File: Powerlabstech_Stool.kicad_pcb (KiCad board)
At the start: 2 copper layers, 75 x 85 mm, 54 parts, among them J1 Screw_Terminal_01x02, J2 Conn_01x02_Pin, J3 Conn_01x02_Pin, J4 Conn_01x05_Socket, J5 Screw_Terminal_01x02, K1 SANYOU_SRD_Form_C, Q1 Q_NMOS_GSD, Q2 Q_NMOS_GSD, Q3 Q_NMOS_GSD, Q4 Q_NMOS_GSD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

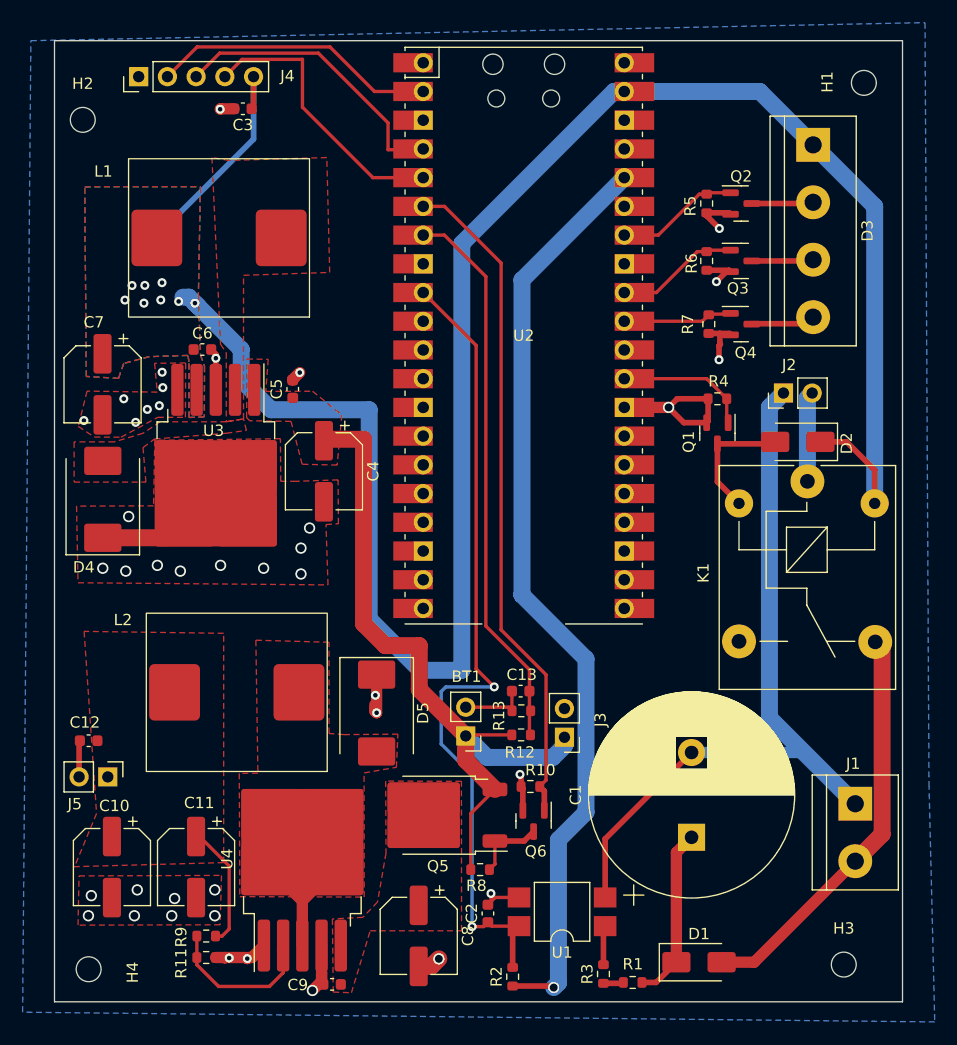
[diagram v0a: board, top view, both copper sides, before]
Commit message: Added the USB output and added the output files
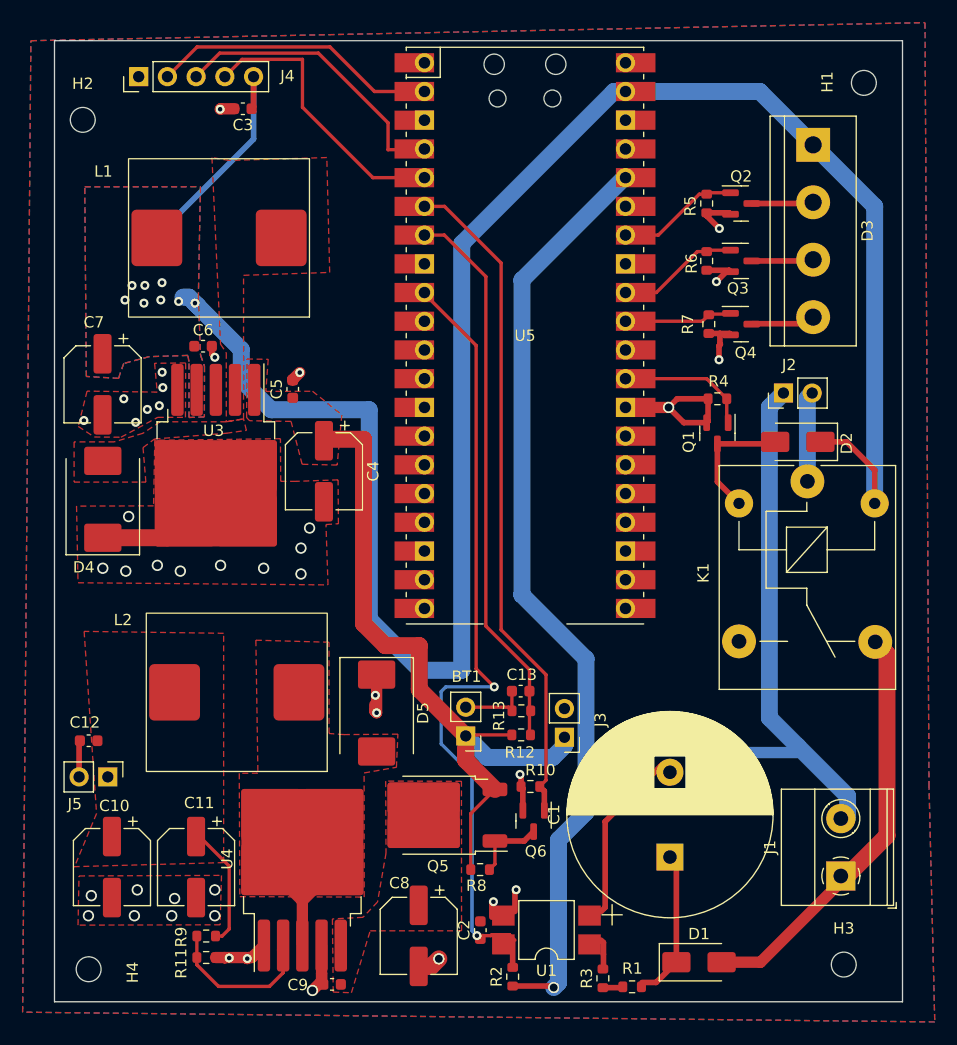
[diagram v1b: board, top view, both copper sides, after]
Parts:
- removed U2: Pi_Pico, footprint_library:RPi_Pico_SMD_TH_REMOVED_SWD_PINS
- added G***: LOGO, LOGO, B.Cu at (89.5, 104.4)
- added U5: SC0915, footprint_library:RPi_Pico_SMD_TH_REMOVED_SWD_PINS, F.Cu at (118.1, 84.6)
- J1: footprint TerminalBlock:TerminalBlock_bornier-2_P5.08mm -> TerminalBlock_Phoenix:TerminalBlock_Phoenix_MKDS-1,5-2-5.08_1x02_P5.08mm_Horizontal
- moved J1 6.52 mm to (146.0, 132.4), turned to 90 degrees
- moved C1 2.59 mm to (130.9, 130.7)
- moved U1 2.12 mm to (120.0, 137.2)
- moved C2 1.62 mm to (114.2, 137.2)
- moved R1 0.39 mm to (127.6, 142.2)
- moved R3 0.39 mm to (125.0, 141.4)
- moved C6 0.30 mm to (89.6, 85.5)
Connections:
- J1 pad 1: /NEUTRAL -> /LIVE
- J1 pad 2: /LIVE -> /NEUTRAL
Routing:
- net GND: track 74.1 -> 70.7 mm, vias 40 -> 41
- net /NEUTRAL: track 65.9 -> 67.5 mm
- net /MAINS_SENSE: track 72.6 -> 71.0 mm
- net /main_det_ret: track 15.4 -> 13.9 mm
- net Net-(R3-Pad2): track 3.47 -> 2.25 mm
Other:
- board text added: "HIGH VOLTAGE"

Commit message: Modified USB type C to supply 3A current
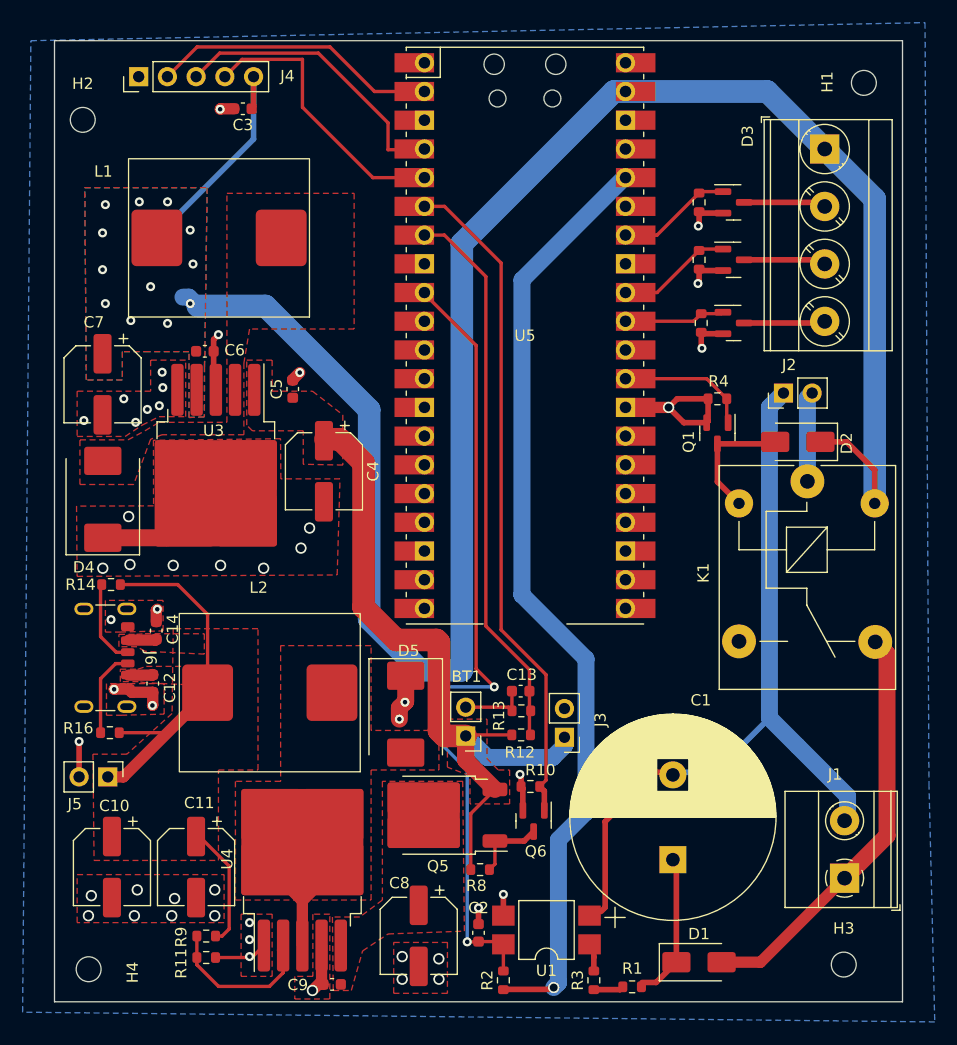
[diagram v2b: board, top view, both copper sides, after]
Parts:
- added C14: 100nF, Capacitor_SMD:C_0603_1608Metric, F.Cu at (85.5, 110.7)
- added J6: USB_C_Receptacle_PowerOnly_6P, Connector_USB:USB_C_Receptacle_GCT_USB4125-xx-x_6P_TopMnt_Horizontal, F.Cu at (79.9, 113.1)
- added R14: 10K, Resistor_SMD:R_0603_1608Metric, F.Cu at (81.5, 106.6)
- added R16: 10K, Resistor_SMD:R_0603_1608Metric, F.Cu at (81.4, 119.7)
- D3: footprint TerminalBlock:TerminalBlock_bornier-4_P5.08mm -> TerminalBlock_Phoenix:TerminalBlock_Phoenix_MKDS-3-4-5.08_1x04_P5.08mm_Horizontal
- moved C12 7.60 mm to (85.2, 115.3), turned to -90 degrees
- moved L2 2.92 mm to (101.0, 116.2)
- moved D5 2.57 mm to (107.6, 118.1)
- moved D3 1.09 mm to (144.6, 68.1)
- moved R2 0.88 mm to (116.2, 141.6)
- moved R3 0.82 mm to (124.2, 141.6)
- moved Q4 0.68 mm to (136.6, 83.5)
- moved R7 0.68 mm to (133.7, 83.5)
- moved Q2 0.68 mm to (136.6, 72.8)
- moved Q3 0.68 mm to (136.6, 77.9)
- moved R5 0.68 mm to (133.5, 72.8)
- moved R6 0.68 mm to (133.5, 77.9)
- moved C6 0.48 mm to (89.8, 86.0)
- moved J1 0.38 mm to (146.4, 132.6)
- moved C1 0.35 mm to (131.2, 130.9)
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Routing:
- net /sw_OUT: track 11.1 -> 52.6 mm
- net Net-(J6-CC2): track 0.00 -> 7.79 mm
- net Net-(J6-CC1): track 0.00 -> 7.59 mm
- net GND: track 70.7 -> 75.6 mm, vias 41 -> 48
- net /LED_RED_OUT: track 5.48 -> 7.27 mm
- net /LED_GREEN_OUT: track 5.48 -> 7.27 mm
- net /LED_BLUE_OUT: track 5.67 -> 7.18 mm
- net +5V: track 192.0 -> 190.8 mm, vias 8 -> 12
- net +3.3V: track 82.4 -> 83.4 mm
- net Net-(R1-Pad2): track 1.79 -> 2.66 mm
- net /LED_BLUE: track 9.70 -> 8.95 mm
- net /LED_GREEN: track 11.0 -> 10.2 mm
- net /LED_RED: track 11.0 -> 10.3 mm
